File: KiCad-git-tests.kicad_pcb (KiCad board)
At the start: 2 copper layers, 0 parts

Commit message: Change the led and create a pcb
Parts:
- added D1: LED_Dual_Bidirectional, LED_SMD:LED_1812_4532Metric_Pad1.30x3.40mm_HandSolder, F.Cu at (68.2, 40.0)
- added R1: R, Resistor_SMD:R_0612_1632Metric, F.Cu at (59.2, 40.2)
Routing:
- net Net-(D1-KA): track 0.00 -> 6.07 mm
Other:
- board outline added: 23 x 11.8 mm

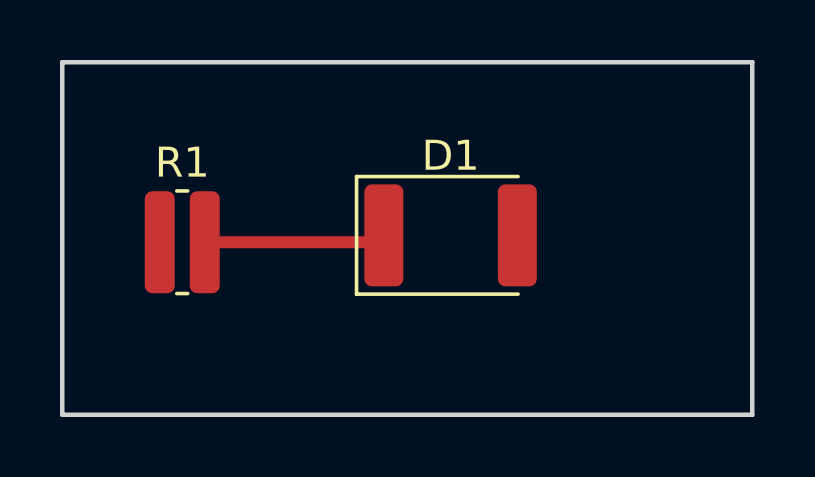
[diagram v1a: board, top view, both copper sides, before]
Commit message: Flip led to test KiRi
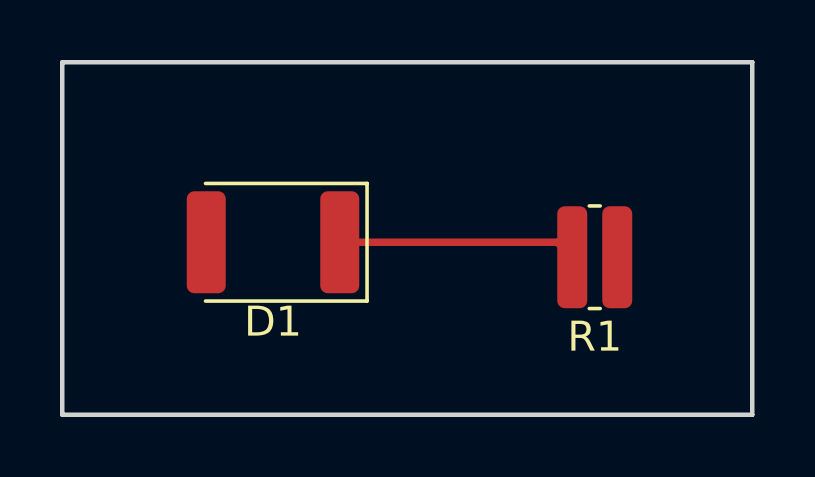
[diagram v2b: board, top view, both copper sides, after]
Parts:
- moved R1 13.8 mm to (73.0, 40.8), turned to 180 degrees
- moved D1 5.92 mm to (62.3, 40.2), turned to 180 degrees
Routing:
- net Net-(D1-KA): track 6.07 -> 7.96 mm
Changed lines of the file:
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@@
 	(footprint "Resistor_SMD:R_0612_1632Metric"
 		(layer "F.Cu")
-		(at 59.25 40.25)
+		(at 73 40.75 180)
 		(descr "Resistor SMD 0612 (1632 Metric), square (rectangular) end terminal, IPC-7351 nominal, (Body size source: https://www.vishay.com/docs/20019/rcwe.pdf)")
 		(tags "resistor")
@@
 		(duplicate_pad_numbers_are_jumpers no)
 		(fp_line
+			(start -0.182983 1.71)
+			(end 0.182983 1.71)
+			(stroke
+				(width 0.12)
+				(type solid)
+			)
+			(layer "F.SilkS")
+		)
+		(fp_line
 			(start -0.182983 -1.71)
 			(end 0.182983 -1.71)
-			(stroke
-				(width 0.12)
-				(type solid)
-			)
-			(layer "F.SilkS")
-		)
-		(fp_line
-			(start -0.182983 1.71)
-			(end 0.182983 1.71)
 			(stroke
 				(width 0.12)
@@
 		)
 		(pad "1" smd roundrect
-			(at -0.75 0)
+			(at -0.75 0 180)
 			(size 1 3.4)
 			(layers "F.Cu" "F.Mask" "F.Paste")
@@
 		)
 		(pad "2" smd roundrect
-			(at 0.75 0)
+			(at 0.75 0 180)
 			(size 1 3.4)
 			(layers "F.Cu" "F.Mask" "F.Paste")
@@
 	(footprint "LED_SMD:LED_1812_4532Metric_Pad1.30x3.40mm_HandSolder"
 		(layer "F.Cu")
-		(at 68.195 40.02)
+		(at 62.275 40.25 180)
 		(descr "LED SMD 1812 (4532 Metric), square (rectangular) end terminal, IPC-7351 nominal, (Body size source: https://www.nikhef.nl/pub/departments/mt/projects/detectorR_D/dtddice/ERJ2G.pdf)")
 		(tags "LED handsolder")
@@
 		(duplicate_pad_numbers_are_jumpers no)
 		(fp_line
+			(start 2.25 -1.96)
+			(end -3.135 -1.96)
+			(stroke
+				(width 0.12)
+				(type solid)
+			)
+			(layer "F.SilkS")
+		)
+		(fp_line
+			(start -3.135 1.96)
+			(end 2.25 1.96)
+			(stroke
+				(width 0.12)
+				(type solid)
+			)
+			(layer "F.SilkS")
+		)
+		(fp_line
 			(start -3.135 -1.96)
 			(end -3.135 1.96)
-			(stroke
-				(width 0.12)
-				(type solid)
-			)
-			(layer "F.SilkS")
-		)
-		(fp_line
-			(start -3.135 1.96)
-			(end 2.25 1.96)
-			(stroke
-				(width 0.12)
-				(type solid)
-			)
-			(layer "F.SilkS")
-		)
-		(fp_line
-			(start 2.25 -1.96)
-			(end -3.135 -1.96)
 			(stroke
 				(width 0.12)
@@
 		)
 		(fp_line
+			(start 2.25 1.6)
+			(end 2.25 -1.6)
+			(stroke
+				(width 0.1)
+				(type solid)
+			)
+			(layer "F.Fab")
+		)
+		(fp_line
+			(start 2.25 -1.6)
+			(end -1.45 -1.6)
+			(stroke
+				(width 0.1)
+				(type solid)
+			)
+			(layer "F.Fab")
+		)
+		(fp_line
+			(start -1.45 -1.6)
+			(end -2.25 -0.8)
+			(stroke
+				(width 0.1)
+				(type solid)
+			)
+			(layer "F.Fab")
+		)
+		(fp_line
+			(start -2.25 1.6)
+			(end 2.25 1.6)
+			(stroke
+				(width 0.1)
+				(type solid)
+			)
+			(layer "F.Fab")
+		)
+		(fp_line
 			(start -2.25 -0.8)
 			(end -2.25 1.6)
@@
 			(layer "F.Fab")
 		)
-		(fp_line
-			(start -2.25 1.6)
-			(end 2.25 1.6)
-			(stroke
-				(width 0.1)
-				(type solid)
-			)
-			(layer "F.Fab")
-		)
-		(fp_line
-			(start -1.45 -1.6)
-			(end -2.25 -0.8)
-			(stroke
-				(width 0.1)
-				(type solid)
-			)
-			(layer "F.Fab")
-		)
-		(fp_line
-			(start 2.25 -1.6)
-			(end -1.45 -1.6)
-			(stroke
-				(width 0.1)
-				(type solid)
-			)
-			(layer "F.Fab")
-		)
-		(fp_line
-			(start 2.25 1.6)
-			(end 2.25 -1.6)
-			(stroke
-				(width 0.1)
-				(type solid)
-			)
-			(layer "F.Fab")
-		)
 		(fp_text user "${REFERENCE}"
 			(at 0 0 0)
@@
 		)
 		(pad "1" smd roundrect
-			(at -2.225 0)
+			(at -2.225 0 180)
 			(size 1.3 3.4)
 			(layers "F.Cu" "F.Mask" "F.Paste")
@@
 		)
 		(pad "2" smd roundrect
-			(at 2.225 0)
+			(at 2.225 0 180)
 			(size 1.3 3.4)
 			(layers "F.Cu" "F.Mask" "F.Paste")
@@
 	)
 	(segment
-		(start 60 40.25)
-		(end 65.74 40.25)
-		(width 0.4)
+		(start 64.5 40.25)
+		(end 71.75 40.25)
+		(width 0.25)
 		(layer "F.Cu")
 		(net "Net-(D1-KA)")
 	)
 	(segment
-		(start 65.74 40.25)
-		(end 65.97 40.02)
-		(width 0.4)
+		(start 71.75 40.25)
+		(end 72.25 40.75)
+		(width 0.25)
 		(layer "F.Cu")
 		(net "Net-(D1-KA)")
